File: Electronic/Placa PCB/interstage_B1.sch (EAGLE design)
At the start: 9 parts, among them J1 0532611271, J3 0532611271, Q1 PMV16XNR, U1 LM70CIMM-3, U2 LM70CIMM-3

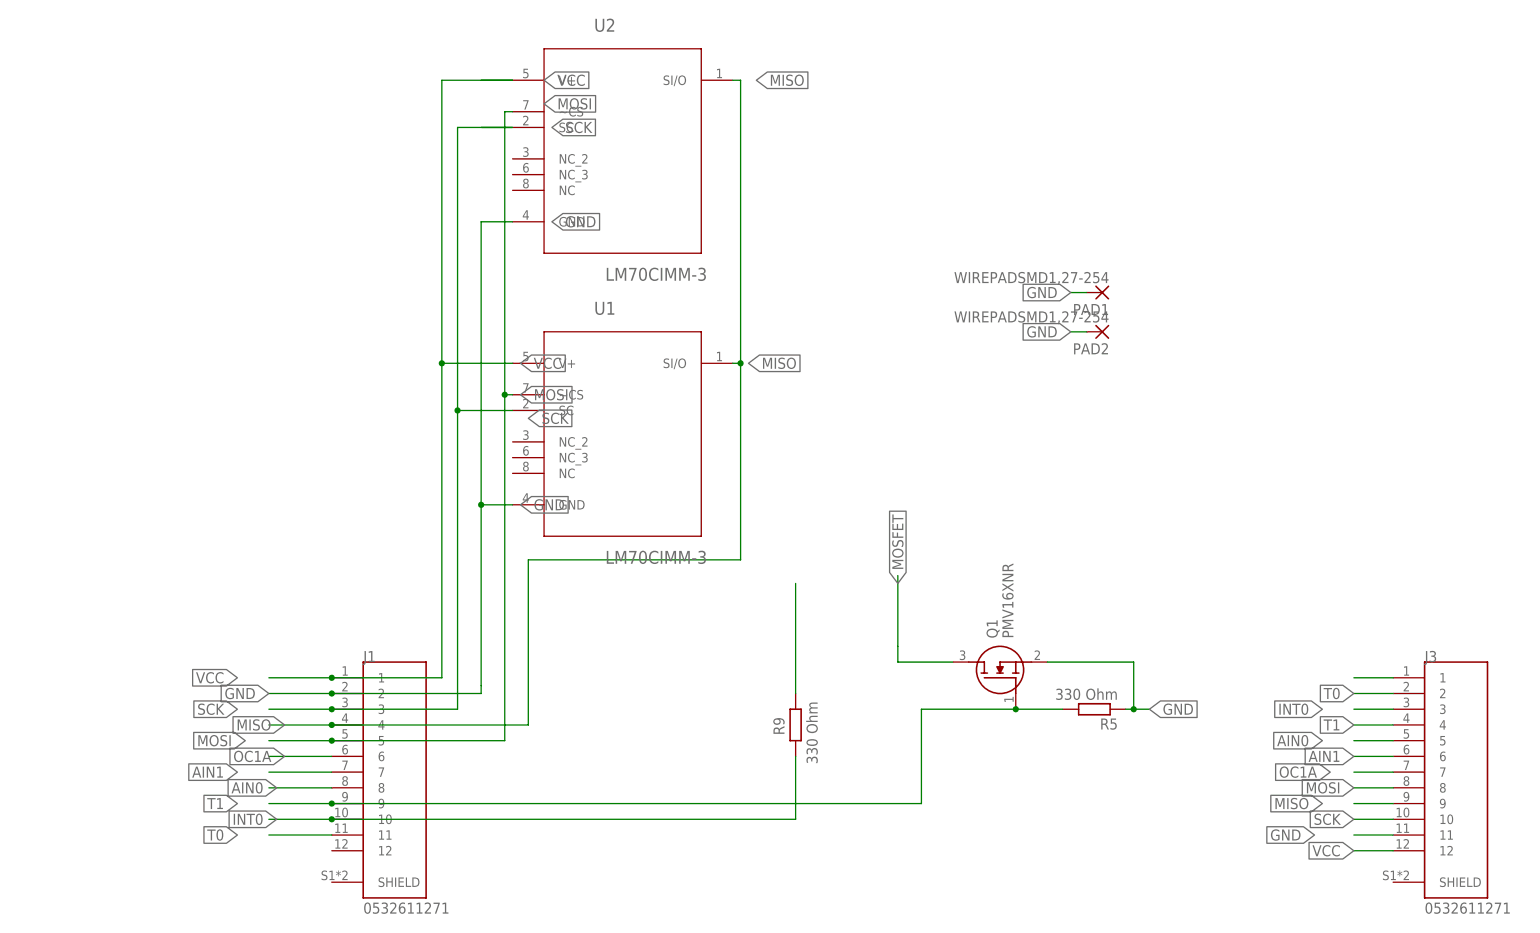
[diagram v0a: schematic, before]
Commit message: Ensamblaje placa
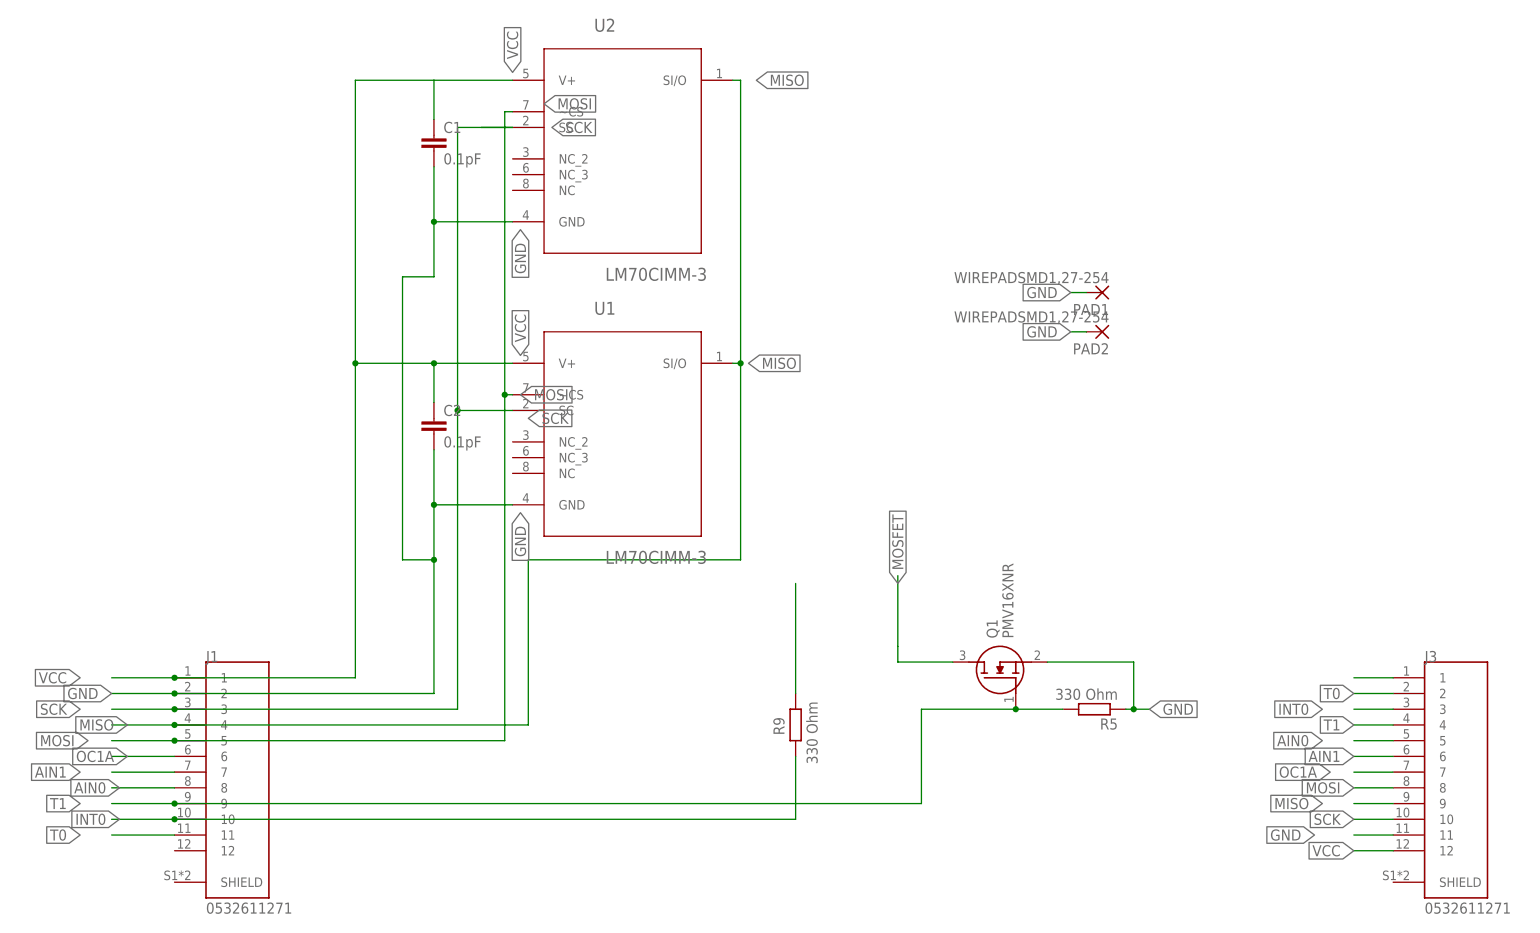
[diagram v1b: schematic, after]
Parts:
- added C1, C2: 0.1pF, rcl:C-EUC0603K
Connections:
- net GND: now also C1.2, C2.2
- net VCC: now also C1.1, C2.1
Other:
- moved on the sheet: J1
